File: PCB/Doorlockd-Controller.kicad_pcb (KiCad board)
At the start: 2 copper layers, 132 x 103 mm, 59 parts, among them J10 Power Out 1, J11 Audio out, J12 GPIO 3, J13 Debug UART, J14 GPIO 4, J15 Power Out 2, J16 to extra screw conn., J18 GPIO only MilkV 1.8V, J19 3V 5V Vin, J20 3V 5V Vin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

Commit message: Added kibot workflow for automatic versioning
see https://github.com/matthijskooijman/PCB-workflows
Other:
- board text added: "${BOARD_REVISION} ${COMPONENTS_DATE}"
- board text removed: "v2.0"

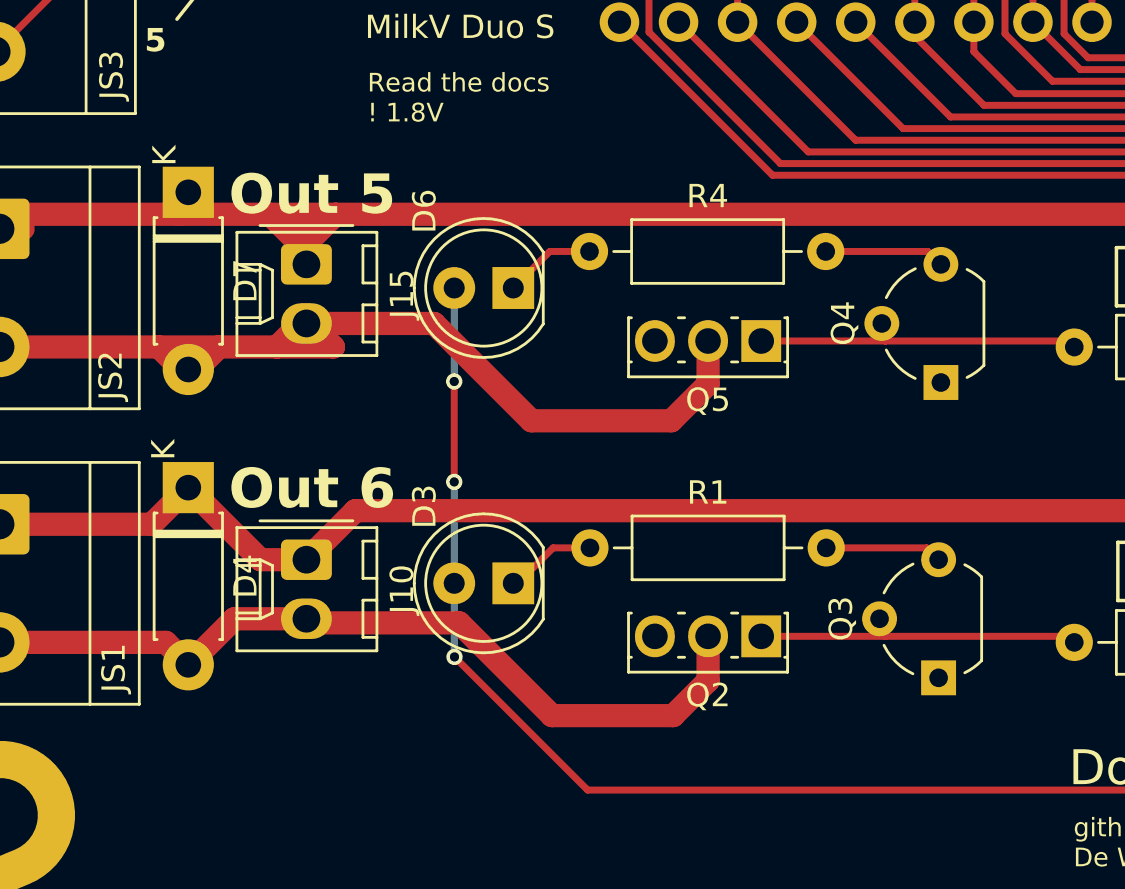
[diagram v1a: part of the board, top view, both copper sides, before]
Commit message: Fixed various ERC rule errors and warnings
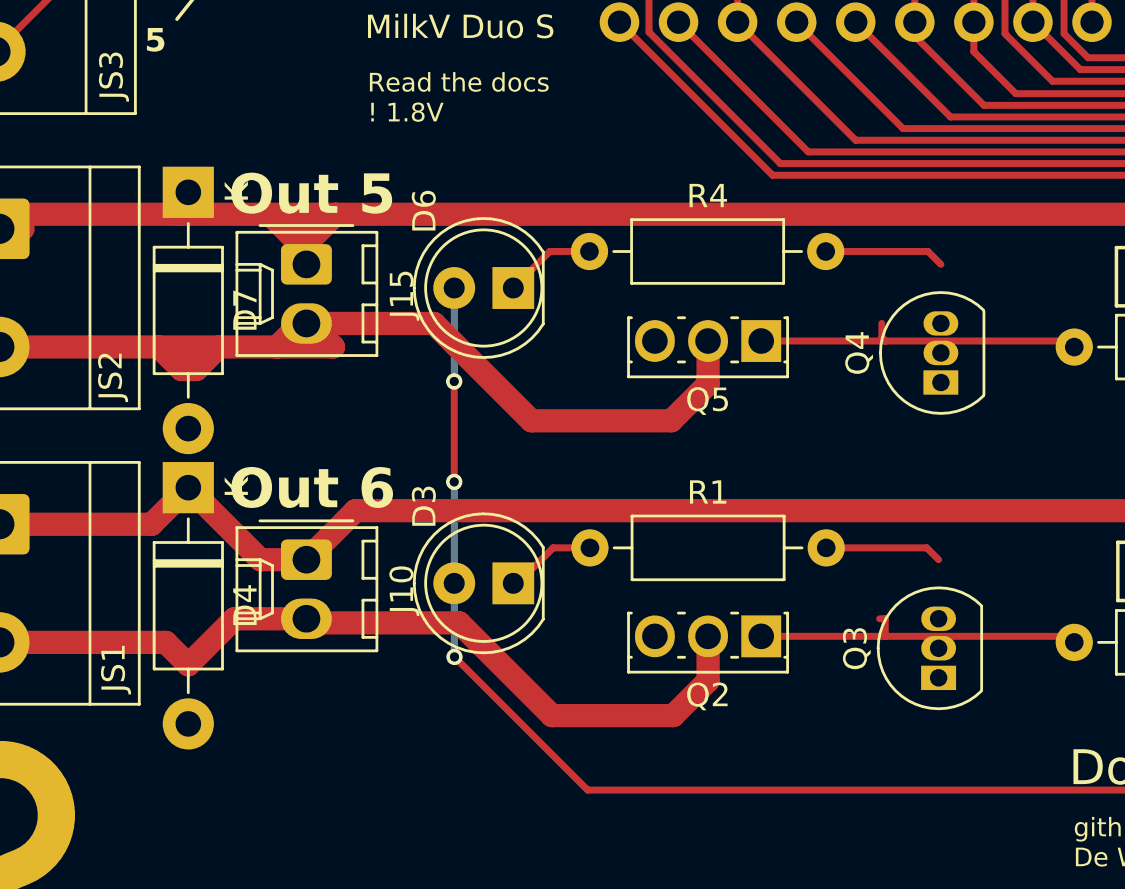
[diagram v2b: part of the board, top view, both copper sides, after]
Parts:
- D4, D7: footprint Diode_THT:D_DO-41_SOD81_P7.62mm_Horizontal -> Diode_THT:D_DO-41_SOD81_P10.16mm_Horizontal
- J11: value Audio out -> DC in
- J5: value AudioJack3 -> Audio out
- Q3, Q4: footprint Package_TO_SOT_THT:TO-92_Wide -> Package_TO_SOT_THT:TO-92_Inline
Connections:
- H1 pad 1: (no net) -> Earth
- H2 pad 1: (no net) -> Earth
- H3 pad 1: (no net) -> Earth
- H4 pad 1: (no net) -> Earth

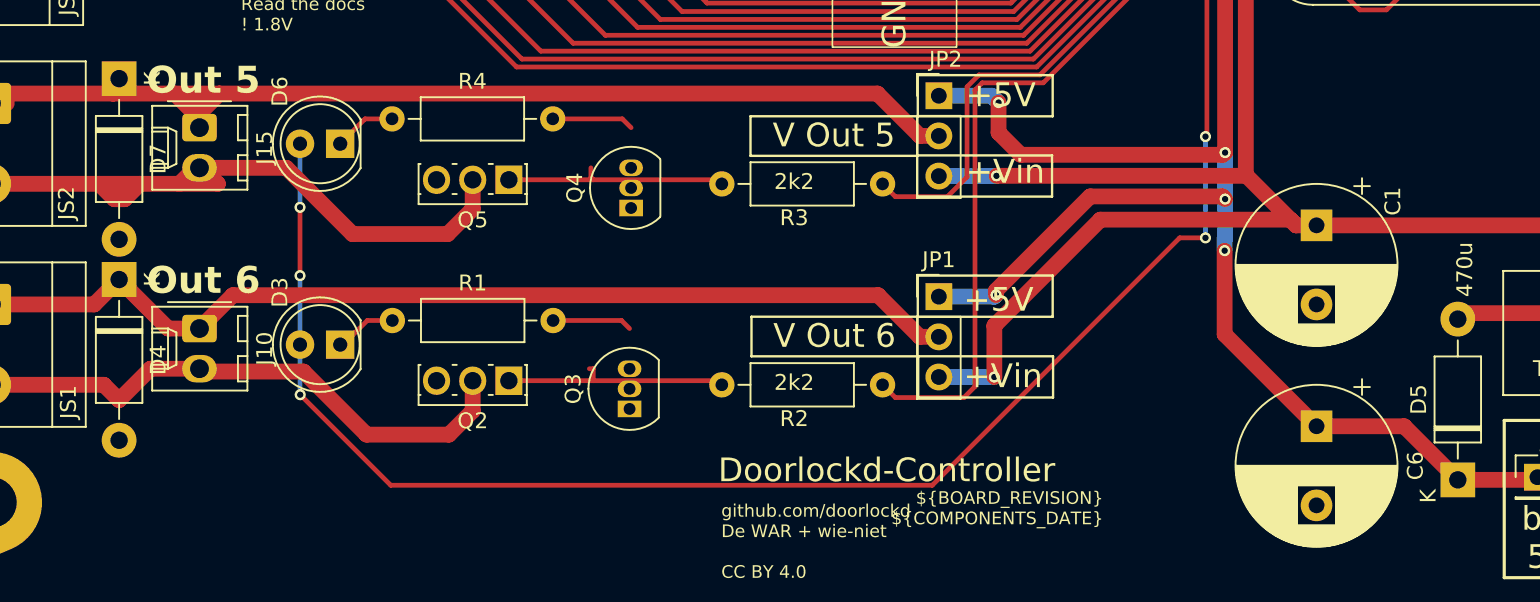
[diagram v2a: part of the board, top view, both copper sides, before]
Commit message: Fixed earlier fixed problems overwritten by last attemp to fix problems
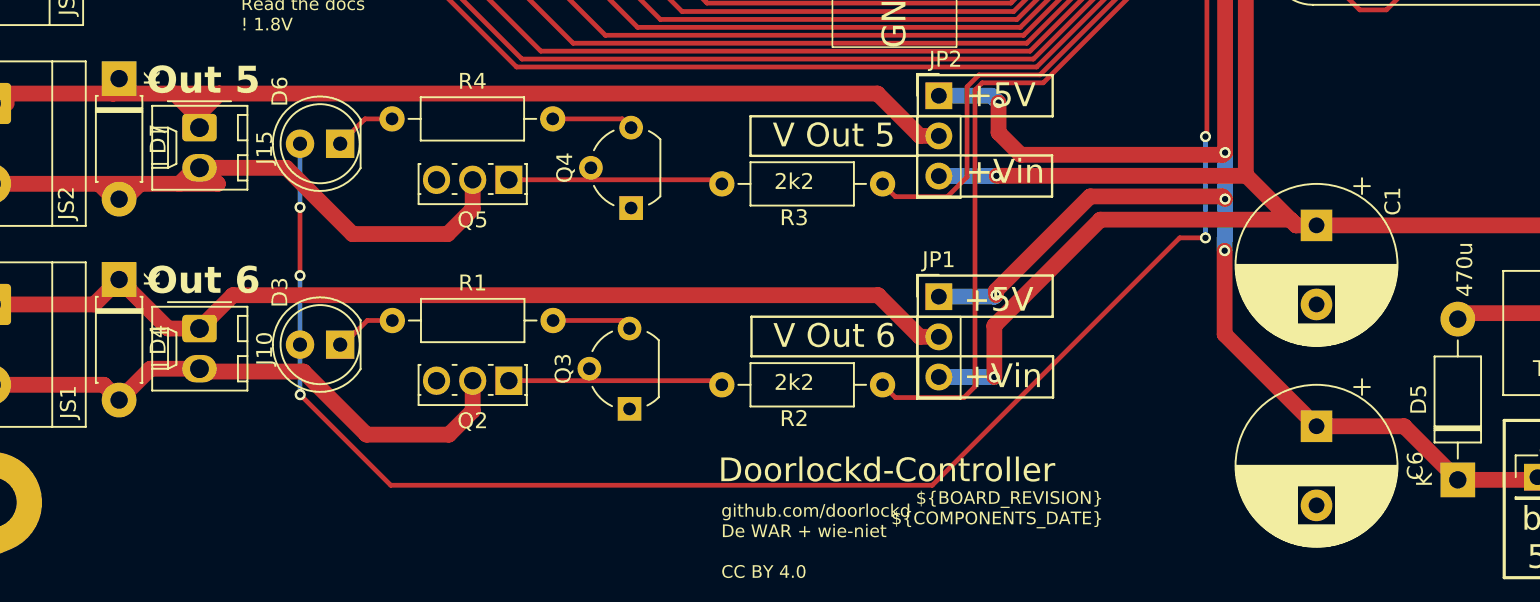
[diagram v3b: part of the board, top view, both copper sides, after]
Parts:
- D4, D7: footprint Diode_THT:D_DO-41_SOD81_P10.16mm_Horizontal -> Diode_THT:D_DO-41_SOD81_P7.62mm_Horizontal
- Q3, Q4: footprint Package_TO_SOT_THT:TO-92_Inline -> Package_TO_SOT_THT:TO-92_Wide
